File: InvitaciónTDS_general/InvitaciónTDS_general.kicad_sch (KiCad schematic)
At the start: 2 parts, among them J1 Conn_01x02_Pin

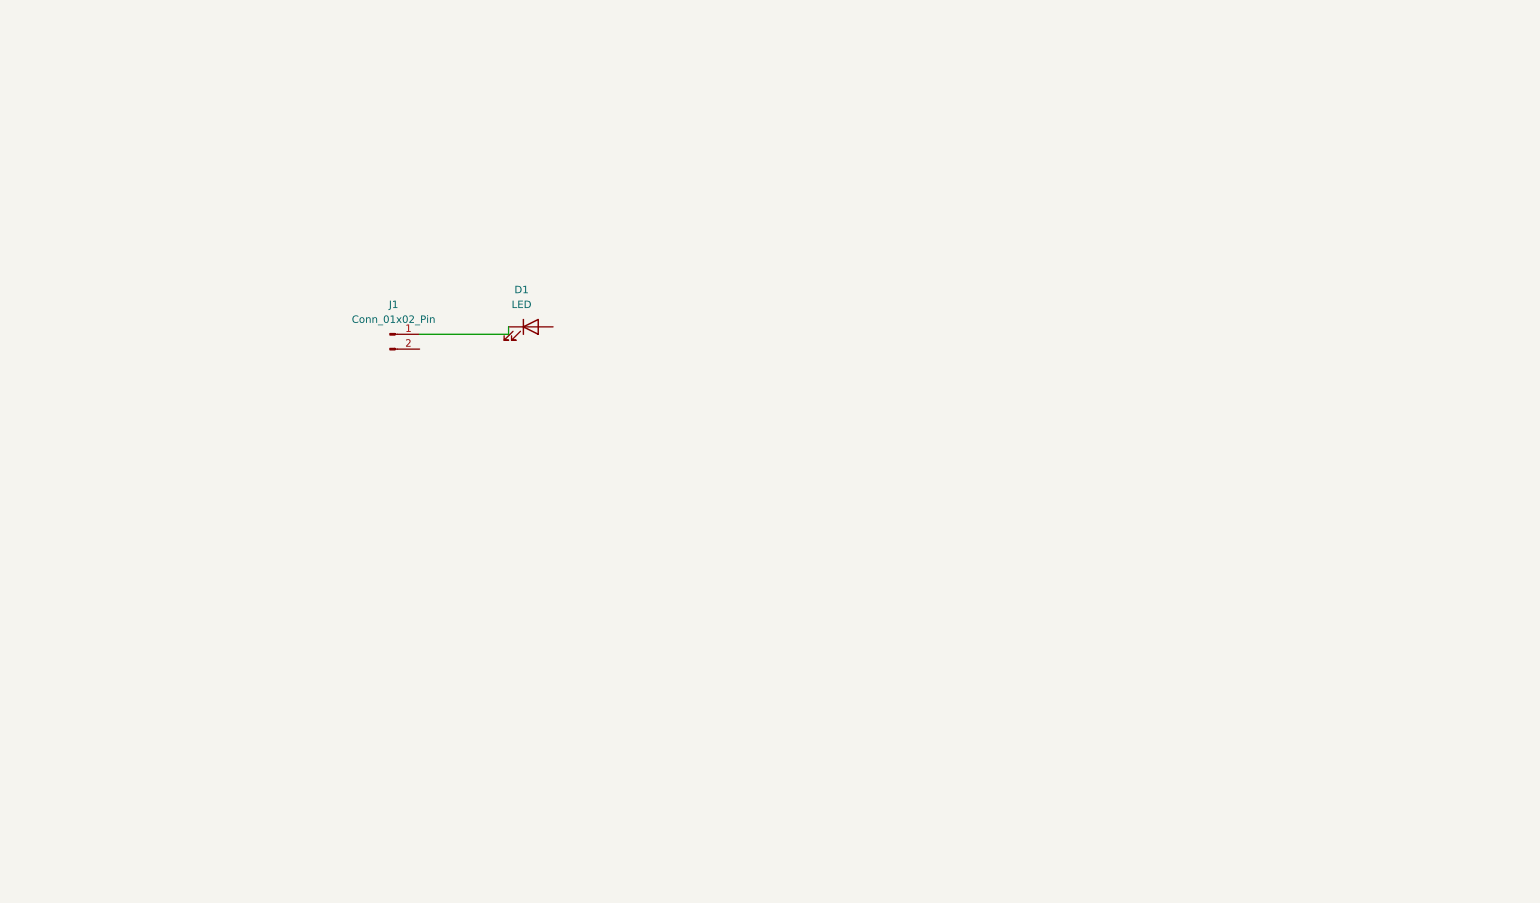
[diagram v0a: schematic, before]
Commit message: Esquemático actualizado, rev 1, pre-retro
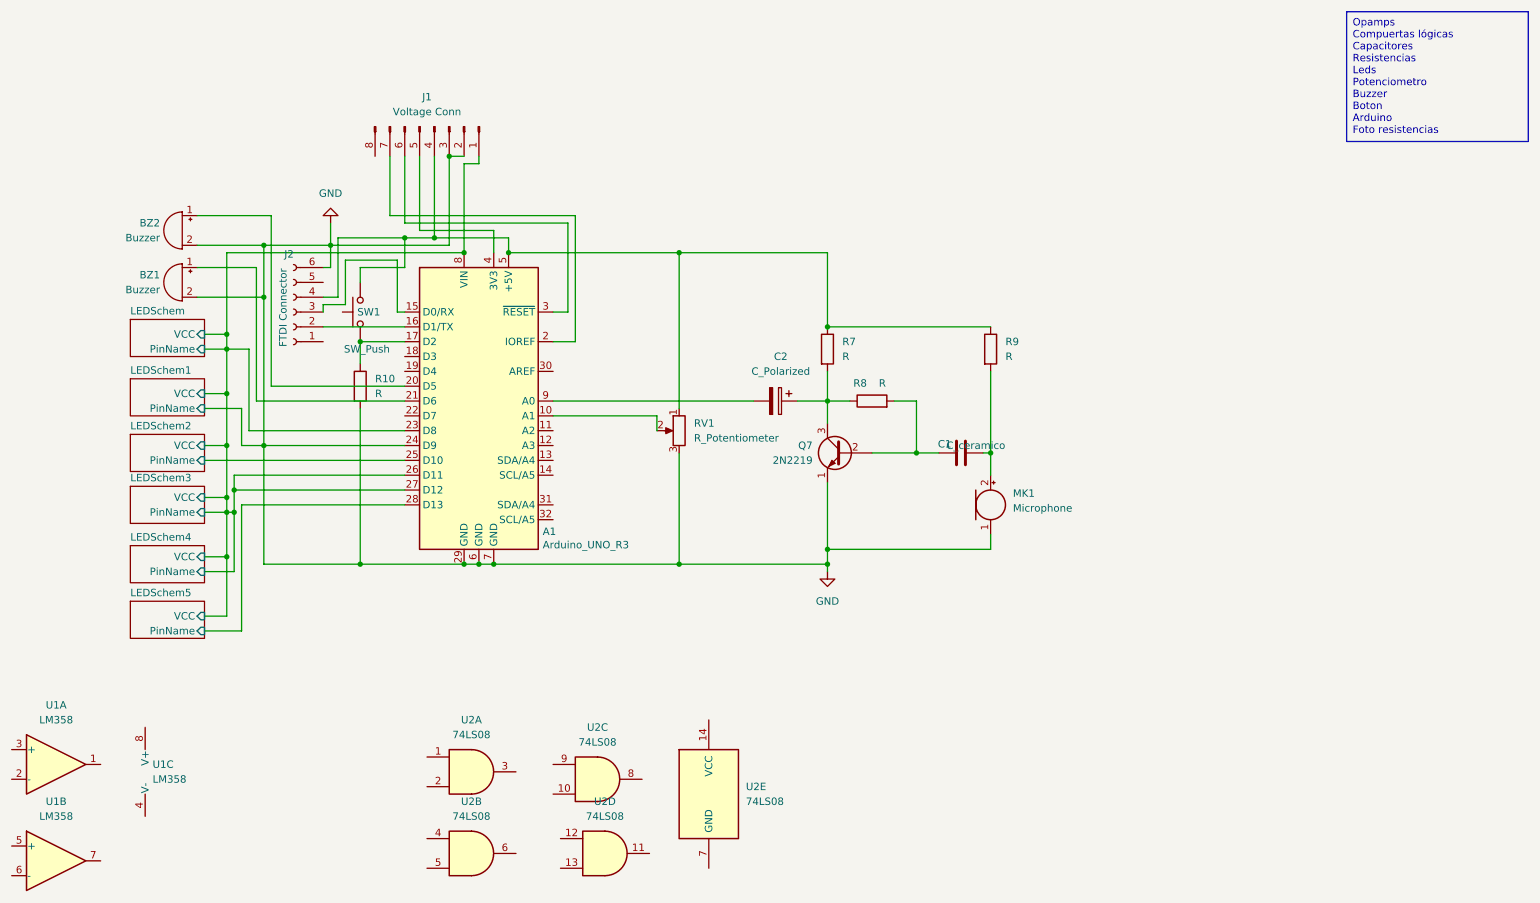
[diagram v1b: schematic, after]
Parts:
- removed D1: LED, LED_THT:LED_D3.0mm, symbol Device:LED
- removed J1: Conn_01x02_Pin, Connector_PinHeader_1.00mm:PinHeader_1x02_P1.00mm_Vertical, symbol Connector:Conn_01x02_Pin
- added A1: Arduino_UNO_R3, Module:Arduino_UNO_R3, symbol MCU_Module:Arduino_UNO_R3
- added BZ1, BZ2: Buzzer, Buzzer_Beeper:Buzzer_12x9.5RM7.6, symbol Device:Buzzer
- added C1: C_ceramico, Capacitor_THT:C_Disc_D3.8mm_W2.6mm_P2.50mm, symbol Device:C
- added C2: C_Polarized, Capacitor_THT:CP_Radial_D6.3mm_P2.50mm, symbol Device:C_Polarized
- added J1: Voltage Conn, Connector_PinHeader_2.54mm:PinHeader_1x08_P2.54mm_Vertical, symbol Connector:Conn_01x08_Pin
- added J2: FTDI Connector, Connector_PinHeader_2.54mm:PinHeader_1x06_P2.54mm_Vertical, symbol Connector:Conn_01x06_Socket
- added MK1: Microphone, Sensor_Audio:POM-2244P-C3310-2-R, symbol Device:Microphone
- added Q7: 2N2219, Package_TO_SOT_THT:TO-39-3, symbol Transistor_BJT:2N2219
- added R10, R7, R8, R9: R, Resistor_THT:R_Axial_DIN0207_L6.3mm_D2.5mm_P10.16mm_Horizontal, symbol Device:R
- added RV1: R_Potentiometer, Potentiometer_THT:Potentiometer_Bourns_3386C_Horizontal, symbol Device:R_Potentiometer
- added SW1: SW_Push, Button_Switch_THT:SW_PUSH_6mm, symbol Switch:SW_Push
- added U1: LM358, Package_DIP:DIP-8_W7.62mm, symbol Amplifier_Operational:LM358
- added U2: 74LS08, Package_DIP:DIP-14_W7.62mm_LongPads, symbol 74xx:74LS08
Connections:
- new net: A1.5 (+5V), J1.4 (Pin_4), J2.4 (Pin_4), R7.1, R9.1, RV1.1, SW1.2
- new net: A1.4 (3V3), J1.5 (Pin_5)
- new net: A1.3 (~{RESET}), J1.6 (Pin_6)
- new net: A1.2 (IOREF), J1.7 (Pin_7)
- new net: C1.2, MK1.2 (+), R9.2
- new net: C1.1, Q7.2 (B), R8.2
- new net: C2.1, Q7.3 (C), R7.2, R8.1
- new net: A1.17 (D2), R10.1, SW1.1
- new net: A1.20 (D5), BZ2.1 (+)
- new net: A1.9 (A0), C2.2
- new net: A1.16 (D1/TX), J2.2 (Pin_2)
- new net: A1.15 (D0/RX), J2.3 (Pin_3)
- new net: A1.10 (A1), RV1.2
- new net: A1.21 (D6), BZ1.1 (+)
- new net GND: A1.24 (D9), A1.29 (GND), A1.6 (GND), A1.7 (GND), BZ1.2 (-), BZ2.2 (-), J1.2 (Pin_2), J1.3 (Pin_3), J2.6 (Pin_6), MK1.1 (-), Q7.1 (E), R10.2, RV1.3
- new net LEDSchem/PinName: A1.23 (D8), A1.26 (D11), A1.27 (D12), A1.8 (VIN), J1.1 (Pin_1)
- new net LEDSchem2/PinName: A1.25 (D10)
- new net LEDSchem5/PinName: A1.28 (D13)
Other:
- added sheet LEDSchem (LEDSchem.kicad_sch)
- added sheet LEDSchem1 (LEDSchem.kicad_sch)
- added sheet LEDSchem2 (LEDSchem.kicad_sch)
- added sheet LEDSchem3 (LEDSchem.kicad_sch)
- added sheet LEDSchem4 (LEDSchem.kicad_sch)
- added sheet LEDSchem5 (LEDSchem.kicad_sch)
